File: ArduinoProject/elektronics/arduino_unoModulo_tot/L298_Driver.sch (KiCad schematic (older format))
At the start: 6 parts, among them U1 L298D, U3 74AHC1G04, U4 74AHC1G04

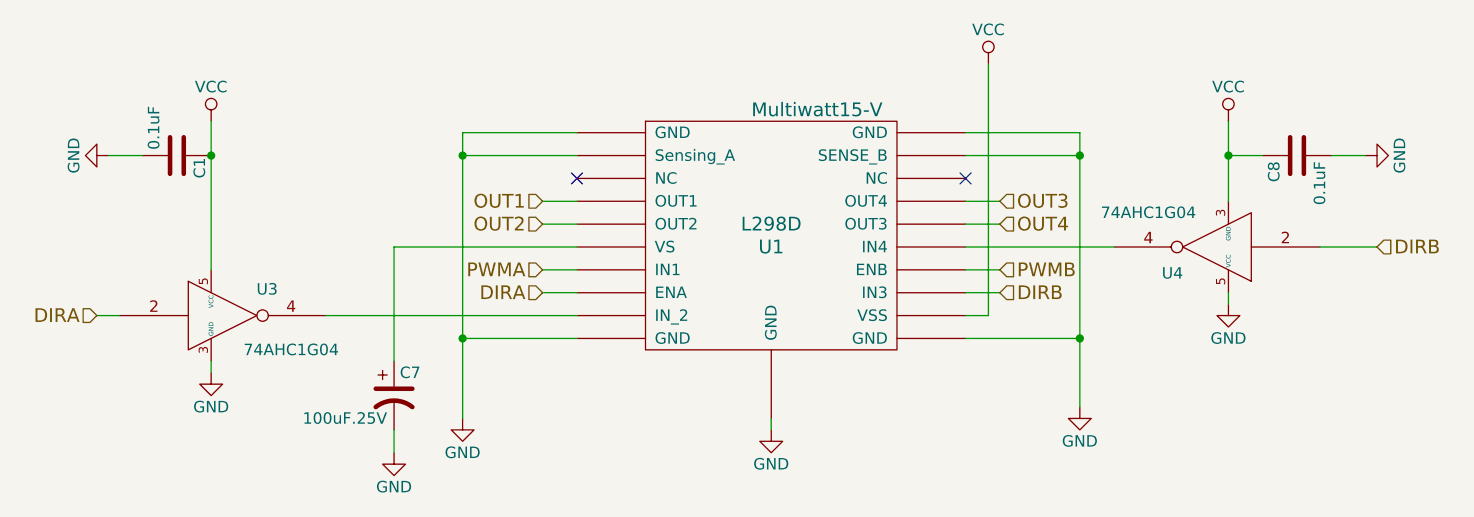
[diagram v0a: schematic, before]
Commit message: kicad schema altered: alles op 1 PCB2
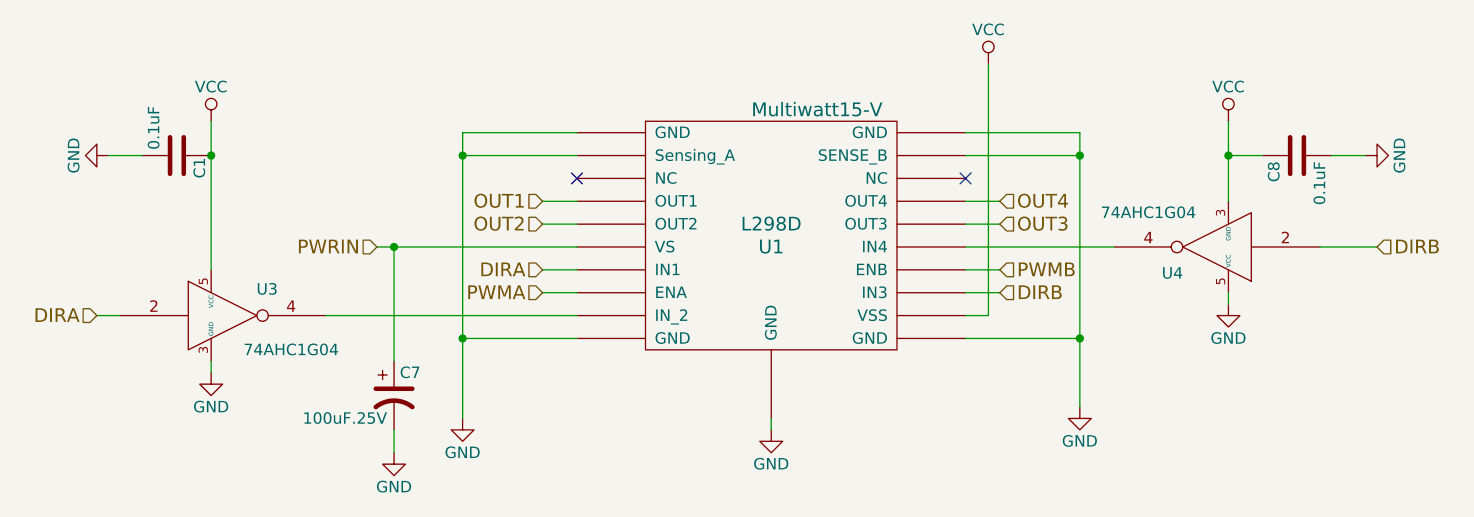
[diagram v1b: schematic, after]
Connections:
- net PWRIN: now reaches C7.1, U1.~ (VSS)
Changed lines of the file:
@@
 	2900 2600 3050 2600
 Wire Wire Line
-	4950 3000 4150 3000
+	4075 3000 4950 3000
 Wire Wire Line
 	4150 3000 4150 3500
@@
 Text HLabel 4800 2900 0    60   Input ~ 0
 OUT2
+Text HLabel 6800 2900 2    60   Input ~ 0
+OUT3
 Text HLabel 6800 2800 2    60   Input ~ 0
-OUT3
-Text HLabel 6800 2900 2    60   Input ~ 0
 OUT4
 Text HLabel 6800 3100 2    60   Input ~ 0
@@
 Text HLabel 2850 3300 0    60   Input ~ 0
 DIRA
-Text HLabel 4800 3200 0    60   Input ~ 0
+Text HLabel 4800 3100 0    60   Input ~ 0
 DIRA
 Wire Wire Line
@@
 Wire Wire Line
 	4950 3100 4800 3100
-Text HLabel 4800 3100 0    60   Input ~ 0
+Text HLabel 4800 3200 0    60   Input ~ 0
 PWMA
 Wire Wire Line
 	7300 3000 6650 3000
+Connection ~ 4150 3000
+Text HLabel 4075 3000 0    60   Input ~ 0
+PWRIN
 $EndSCHEMATC
